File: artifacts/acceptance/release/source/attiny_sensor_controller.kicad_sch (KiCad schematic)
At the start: 10 parts, among them J1 QWIIC, J2 UPDI_VTREF_SENSE, U1 ATtiny402-SS, U2 TMP102B

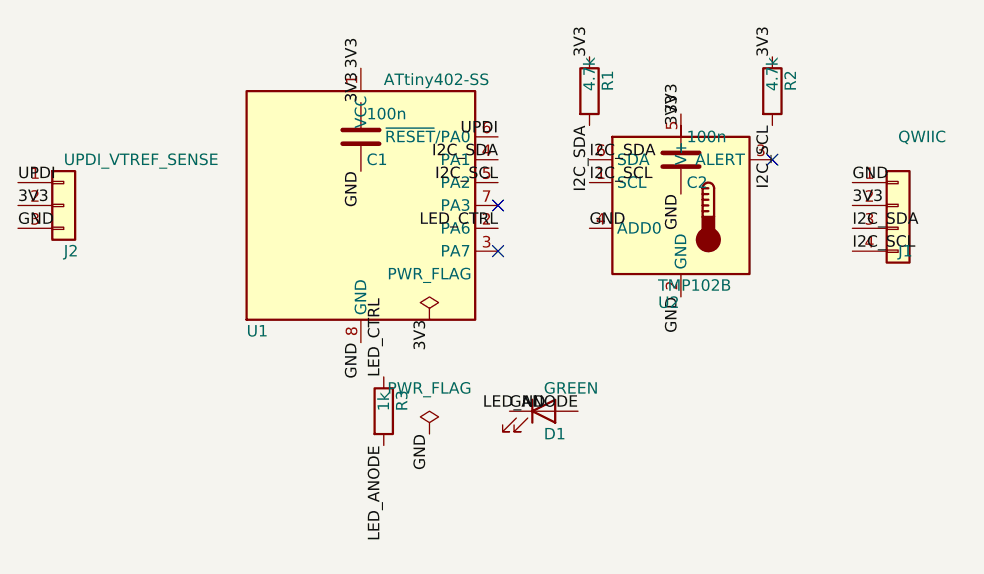
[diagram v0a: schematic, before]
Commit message: refactor: rename PCB Agent to CopperWright
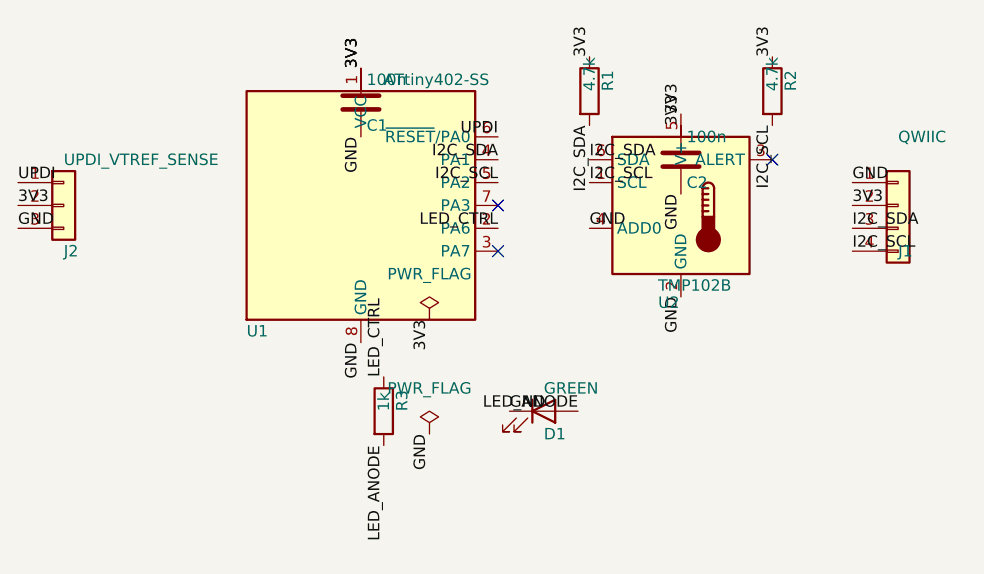
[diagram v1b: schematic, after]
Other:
- company: Generated by pcb-agent-runtime -> Generated by CopperWright
- moved on the sheet: C1
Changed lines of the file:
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@@
 (kicad_sch
 	(version 20250114)
-	(generator "pcb_agent_runtime")
-	(generator_version "0.2.0")
+	(generator "copperwright")
+	(generator_version "1.0.0")
 	(paper "A4")
 	(title_block
 		(title "ATtiny temperature controller")
 		(rev "1.0")
-		(company "Generated by pcb-agent-runtime")
+		(company "Generated by CopperWright")
 	)
 	(symbol
@@
 	(symbol
 		(lib_id "Device:C")
-		(at 63.5 50.8 0)
+		(at 63.5 46.99 0)
 		(unit 1)
 		(exclude_from_sim no)
@@
 		(fields_autoplaced no)
 		(property "Reference" "C1"
-			(at 64.135 53.34 0.0000)
+			(at 64.135 49.53 0.0000)
 			(effects
 				(font
@@
 		)
 		(property "Value" "100n"
-			(at 64.135 48.26 0.0000)
+			(at 64.135 44.45 0.0000)
 			(effects
 				(font
@@
 		)
 		(property "Footprint" "Capacitor_SMD:C_0603_1608Metric"
-			(at 64.4652 46.99 0.0000)
+			(at 64.4652 43.18 0.0000)
 			(effects
 				(font
@@
 		)
 		(property "Manufacturer" "Murata Manufacturing"
-			(at 66.04 55.8799 0)
+			(at 66.04 52.0699 0)
 			(effects
 				(font
@@
 		)
 		(property "MPN" "GRM188R71C104KA01D"
-			(at 66.04 55.8799 0)
+			(at 66.04 52.0699 0)
 			(effects
 				(font
@@
 		)
 		(property "Part_ID" "murata.grm188r71c104ka01d"
-			(at 66.04 55.8799 0)
+			(at 66.04 52.0699 0)
 			(effects
 				(font
@@
 		)
 		(property "Lifecycle" "active"
-			(at 66.04 55.8799 0)
+			(at 66.04 52.0699 0)
 			(effects
 				(font
@@
 		)
 		(property "Trust" "rule_validated"
-			(at 66.04 55.8799 0)
+			(at 66.04 52.0699 0)
 			(effects
 				(font
@@
 		)
 		(property "Datasheet" "https://www.murata.com/en-global/products/productdetail?partno=GRM188R71C104KA01%23"
-			(at 63.5 50.8 0)
+			(at 63.5 46.99 0)
 			(effects
 				(font
@@
 		)
 		(property "Description" "100 nF 10% 16 V X7R 0603 ceramic capacitor"
-			(at 63.5 50.8 0)
+			(at 63.5 46.99 0)
 			(effects
 				(font
@@
 	)
 	(label "3V3"
-		(at 63.5 46.99 90)
+		(at 63.5 43.18 90)
 		(effects
 			(font
@@
 	)
 	(label "GND"
-		(at 63.5 54.61 270)
+		(at 63.5 50.8 270)
 		(effects
 			(font

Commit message: feat: launch PCBDraft AI PCB agent
Build the modular Python agent runtime and TUI, deterministic KiCad generation and repair loop, DeepSeek Harness boundary, qualification gates, release evidence, and the complete PCBDraft brand.
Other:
- company: Generated by CopperWright -> Generated by PCBDraft
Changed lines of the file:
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@@
 (kicad_sch
 	(version 20250114)
-	(generator "copperwright")
+	(generator "pcbdraft")
 	(generator_version "1.0.0")
 	(paper "A4")
@@
 		(title "ATtiny temperature controller")
 		(rev "1.0")
-		(company "Generated by CopperWright")
+		(company "Generated by PCBDraft")
 	)
 	(symbol
